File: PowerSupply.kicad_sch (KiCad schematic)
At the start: 8 parts, among them U301 TPSM33625

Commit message: Update parts
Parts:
- C301: footprint Capacitor_SMD:C_1210_3225Metric -> V2_Capacitor_SMD:C_1210; symbol Device:C_Small -> V2_Device:C_1210_10u; Manufacturer (none) -> TDK; Mouser (none) -> 810-CNA6P1X7R1H106K2; Product (none) -> CNA6P1X7R1H106K250AE; Rating (none) -> 50V; Voltage (none) -> 50V
- C302: footprint Capacitor_SMD:C_0603_1608Metric -> V2_Capacitor_SMD:C_0603; symbol Device:C_Small -> V2_Device:C_0603_0u1; Manufacturer (none) -> TDK; Mouser (none) -> 810-CGA3E2X7R1H104MA; Product (none) -> CGA3E2X7R1H104M080AA
- C303, C304: footprint Capacitor_SMD:C_1210_3225Metric -> V2_Capacitor_SMD:C_1210; symbol Device:C_Small -> V2_Device:C_1210_22u; Manufacturer (none) -> TDK; Mouser (none) -> 810-CGA6P3X7R1E226M5; Product (none) -> CGA6P3X7R1E226M250AE; Rating (none) -> 25V; Voltage (none) -> 25V
- C305: footprint Capacitor_SMD:C_0603_1608Metric -> V2_Capacitor_SMD:C_0603; symbol Device:C_Small -> V2_Device:C_0603_1u; Manufacturer (none) -> YAGEO; Mouser (none) -> 603-CC603KRX7R9BB105; Product (none) -> CC0603KRX7R9BB105
- R301: footprint Resistor_SMD:R_0603_1608Metric -> V2_Resistor_SMD:R_0603; symbol Device:R_Small -> V2_Device:R_0603_40k2; Manufacturer (none) -> Vishay; Mouser (none) -> 71-RCS060340K2FKEA; Product (none) -> RCS060340K2FKEA; Rating (none) -> 500mW
- R302: footprint Resistor_SMD:R_0603_1608Metric -> V2_Resistor_SMD:R_0603; symbol Device:R_Small -> V2_Device:R_0603_10k; Manufacturer (none) -> Vishay; Mouser (none) -> 71-CRCW060310K0FKEAC; Product (none) -> CRCW060310K0FKEAC; Rating (none) -> 100mW
- U301: Manufacturer (none) -> Texas Instruments; Mouser (none) -> 595-TPSM33625RDNR; Product (none) -> TPSM33625RDNR

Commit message: Update library
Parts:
- C301: Voltage 50V -> (none)
- C302: Rating (none) -> 50V
- C303, C304: Voltage 25V -> (none)
- C305: Manufacturer YAGEO -> TDK; Mouser 603-CC603KRX7R9BB105 -> 810-CGA3E3X7R1H105K0; Product CC0603KRX7R9BB105 -> CGA3E3X7R1H105K080AB; Rating (none) -> 50V
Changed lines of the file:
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@@
-			)
-		)
-		(property "Sim.Pin" ""
-			(at 148.59 102.87 0)
-			(effects
-				(font
-					(size 1.27 1.27)
-				)
-				(hide yes)
 			)
 		)
@@
 			)
 		)
-		(property "Sim.Pin" ""
-			(at 109.22 97.79 0)
-			(effects
-				(font
-					(size 1.27 1.27)
-				)
-				(hide yes)
-			)
-		)
 		(property "Manufacturer" "TDK"
 			(at 109.22 113.03 0)
@@
 			)
 		)
+		(property "Rating" "50V"
+			(at 109.22 120.65 0)
+			(effects
+				(font
+					(size 1.27 1.27)
+				)
+				(hide yes)
+			)
+		)
 		(pin "1"
 		)
@@
 			)
 		)
-		(property "Sim.Pin" ""
-			(at 195.58 97.79 0)
-			(effects
-				(font
-					(size 1.27 1.27)
-				)
-				(hide yes)
-			)
-		)
 		(property "Product" "CGA6P3X7R1E226M250AE"
 			(at 195.58 115.57 0)
@@
 			)
 		)
-		(property "Voltage" "25V"
-			(at 195.58 118.11 0)
-			(effects
-				(font
-					(size 1.27 1.27)
-				)
-				(hide yes)
-			)
-		)
 		(pin "1"
 		)
@@
 			)
 		)
-		(property "Sim.Pin" ""
-			(at 172.72 97.79 0)
-			(effects
-				(font
-					(size 1.27 1.27)
-				)
-				(hide yes)
-			)
-		)
 		(property "Rating" "500mW"
 			(at 172.72 118.11 0)
@@
 			)
 		)
-		(property "Description" "Power symbol creates a global label with name \"GND\" , ground"
+		(property "Description" ""
 			(at 185.42 100.33 0)
 			(effects
@@
 			)
 		)
-		(property "Description" "Power symbol creates a global label with name \"GND\" , ground"
+		(property "Description" ""
 			(at 195.58 100.33 0)
 			(effects
@@
 			)
 		)
-		(property "Description" "Power symbol creates a global label with name \"+5V\""
+		(property "Description" ""
 			(at 195.58 95.25 0)
 			(effects
@@
 			)
 		)
-		(property "Description" "Power symbol creates a global label with name \"GND\" , ground"
+		(property "Description" ""
 			(at 97.79 100.33 0)
 			(effects
@@
 			)
 		)
-		(property "Description" "Power symbol creates a global label with name \"GND\" , ground"
+		(property "Description" ""
 			(at 172.72 105.41 0)
 			(effects
@@
 			)
 		)
-		(property "Description" "Power symbol creates a global label with name \"GND\" , ground"
+		(property "Description" ""
 			(at 109.22 100.33 0)
 			(effects
@@
 			)
 		)
-		(property "Mouser" "603-CC603KRX7R9BB105"
+		(property "Mouser" "810-CGA3E3X7R1H105K0"
 			(at 128.27 125.222 0)
 			(effects
@@
 			)
 		)
-		(property "Sim.Pin" ""
-			(at 128.27 107.95 0)
-			(effects
-				(font
-					(size 1.27 1.27)
-				)
-				(hide yes)
-			)
-		)
-		(property "Product" "CC0603KRX7R9BB105"
+		(property "Product" "CGA3E3X7R1H105K080AB"
 			(at 128.27 125.73 0)
 			(effects
@@
 			)
 		)
-		(property "Manufacturer" "YAGEO"
+		(property "Manufacturer" "TDK"
 			(at 128.27 123.19 0)
+			(effects
+				(font
+					(size 1.27 1.27)
+				)
+				(hide yes)
+			)
+		)
+		(property "Rating" "50V"
+			(at 128.27 130.81 0)
 			(effects
 				(font
@@
 			)
 		)
-		(property "Sim.Pin" ""
-			(at 185.42 97.79 0)
-			(effects
-				(font
-					(size 1.27 1.27)
-				)
-				(hide yes)
-			)
-		)
 		(property "Product" "CGA6P3X7R1E226M250AE"
 			(at 185.42 115.57 0)
@@
 			)
 		)
-		(property "Voltage" "25V"
-			(at 185.42 118.11 0)
-			(effects
-				(font
-					(size 1.27 1.27)
-				)
-				(hide yes)
-			)
-		)
 		(pin "1"
 		)
@@
 			)
 		)
-		(property "Description" "Power symbol creates a global label with name \"GND\" , ground"
+		(property "Description" ""
 			(at 128.27 110.49 0)
 			(effects
@@
 			)
 		)
-		(property "Sim.Pin" ""
-			(at 172.72 102.87 0)
-			(effects
-				(font
-					(size 1.27 1.27)
-				)
-				(hide yes)
-			)
-		)
 		(property "Product" "CRCW060310K0FKEAC"
 			(at 172.72 120.65 0)
@@
 			)
 		)
-		(property "Description" "Power symbol creates a global label with name \"GND\" , ground"
+		(property "Description" ""
 			(at 148.59 115.57 0)
 			(effects
@@
 			)
 		)
-		(property "Sim.Pin" ""
-			(at 97.79 97.79 0)
-			(effects
-				(font
-					(size 1.27 1.27)
-				)
-				(hide yes)
-			)
-		)
 		(property "Product" "CNA6P1X7R1H106K250AE"
 			(at 97.79 115.57 0)
@@
 			(effects
 				(font
-					(size 1.27 1.27)
-				)
-				(hide yes)
-			)
-		)
-		(property "Voltage" "50V"
-			(at 97.79 118.11 0)
-			(effects
-				(font

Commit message: Update library
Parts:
- U301: footprint V2_Converter_DCDC:TPSM33625 -> V2_Converter_DCDC:QFN-11; symbol V2_Converter_DCDC:TPSM33625 -> V2_Converter_DCDC:TPSM33625RDNR; Rating (none) -> 2.5A
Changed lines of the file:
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@@
 	)
 	(symbol
-		(lib_id "V2_Converter_DCDC:TPSM33625")
+		(lib_id "V2_Converter_DCDC:TPSM33625RDNR")
 		(at 148.59 102.87 0)
 		(unit 1)
@@
 			)
 		)
-		(property "Footprint" "V2_Converter_DCDC:TPSM33625"
+		(property "Footprint" "V2_Converter_DCDC:QFN-11"
 			(at 148.59 118.11 0)
 			(effects
@@
 			)
 		)
-		(property "Datasheet" "https://www.ti.com/lit/ds/symlink/tpsm33625.pdf"
+		(property "Datasheet" ""
 			(at 153.67 118.11 0)
 			(effects
@@
 			(effects
 				(font
+					(size 1.27 1.27)
+				)
+				(hide yes)
+			)
+		)
+		(property "Rating" "2.5A"
+			(at 148.59 153.67 0)
+			(effects
+				(font

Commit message: Update Library
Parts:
- C301: symbol V2_Device:C_1210_10u -> V2_Capacitor:1210_10u
- C302: symbol V2_Device:C_0603_0u1 -> V2_Capacitor:0603_0u1
- C303, C304: symbol V2_Device:C_1210_22u -> V2_Capacitor:1210_22u
- C305: symbol V2_Device:C_0603_1u -> V2_Capacitor:0603_1u
- R301: symbol V2_Device:R_0603_40k2 -> V2_Resistor:0603_40k2
- R302: symbol V2_Device:R_0603_10k -> V2_Resistor:0603_10k
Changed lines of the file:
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@@
 	)
 	(symbol
-		(lib_id "V2_Device:C_0603_0u1")
+		(lib_id "V2_Capacitor:0603_0u1")
 		(at 109.22 97.79 0)
 		(unit 1)
@@
 	)
 	(symbol
-		(lib_id "V2_Device:C_1210_22u")
+		(lib_id "V2_Capacitor:1210_22u")
 		(at 195.58 97.79 0)
 		(unit 1)
@@
 	)
 	(symbol
-		(lib_id "V2_Device:R_0603_40k2")
+		(lib_id "V2_Resistor:0603_40k2")
 		(at 172.72 97.79 0)
 		(unit 1)
@@
 	)
 	(symbol
-		(lib_id "V2_Device:C_0603_1u")
+		(lib_id "V2_Capacitor:0603_1u")
 		(at 128.27 107.95 0)
 		(unit 1)
@@
 	)
 	(symbol
-		(lib_id "V2_Device:C_1210_22u")
+		(lib_id "V2_Capacitor:1210_22u")
 		(at 185.42 97.79 0)
 		(unit 1)
@@
 	)
 	(symbol
-		(lib_id "V2_Device:R_0603_10k")
+		(lib_id "V2_Resistor:0603_10k")
 		(at 172.72 102.87 0)
 		(unit 1)
@@
 	)
 	(symbol
-		(lib_id "V2_Device:C_1210_10u")
+		(lib_id "V2_Capacitor:1210_10u")
 		(at 97.79 97.79 0)
 		(unit 1)

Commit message: Replace diode
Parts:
- C301: Mouser 810-CNA6P1X7R1H106K2 -> 810-CNC6P1X7R1H106K2; Product CNA6P1X7R1H106K250AE -> CNC6P1X7R1H106K250AE
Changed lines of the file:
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@@
 			)
 		)
-		(property "Description" "Unpolarized capacitor, small symbol"
+		(property "Description" ""
 			(at 109.22 111.252 0)
 			(effects
@@
 			)
 		)
-		(property "Description" "Unpolarized capacitor, small symbol"
+		(property "Description" ""
 			(at 195.58 111.252 0)
 			(effects
@@
 			)
 		)
-		(property "Description" "Resistor, small symbol"
+		(property "Description" ""
 			(at 172.72 109.982 0)
 			(effects
@@
 		(on_board yes)
 		(dnp no)
-		(property "Reference" "#PWR0304"
+		(property "Reference" "#PWR304"
 			(at 185.42 106.68 0)
 			(effects
@@
 			(project "hihat-1"
 				(path "/6c8448b4-b04d-47e1-934e-e40cbe27a7be/db9f305d-c851-4b73-b2af-61e94839e399"
-					(reference "#PWR0304")
+					(reference "#PWR304")
 					(unit 1)
 				)
@@
 		(on_board yes)
 		(dnp no)
-		(property "Reference" "#PWR0305"
+		(property "Reference" "#PWR305"
 			(at 195.58 106.68 0)
 			(effects
@@
 			(project "hihat-1"
 				(path "/6c8448b4-b04d-47e1-934e-e40cbe27a7be/db9f305d-c851-4b73-b2af-61e94839e399"
-					(reference "#PWR0305")
+					(reference "#PWR305")
 					(unit 1)
 				)
@@
 		(on_board yes)
 		(dnp no)
-		(property "Reference" "#PWR0301"
+		(property "Reference" "#PWR301"
 			(at 195.58 99.06 0)
 			(effects
@@
 			(project "hihat-1"
 				(path "/6c8448b4-b04d-47e1-934e-e40cbe27a7be/db9f305d-c851-4b73-b2af-61e94839e399"
-					(reference "#PWR0301")
+					(reference "#PWR301")
 					(unit 1)
 				)
@@
 		(on_board yes)
 		(dnp no)
-		(property "Reference" "#PWR0302"
+		(property "Reference" "#PWR302"
 			(at 97.79 106.68 0)
 			(effects
@@
 			(project "hihat-1"
 				(path "/6c8448b4-b04d-47e1-934e-e40cbe27a7be/db9f305d-c851-4b73-b2af-61e94839e399"
-					(reference "#PWR0302")
+					(reference "#PWR302")
 					(unit 1)
 				)
@@
 		(on_board yes)
 		(dnp no)
-		(property "Reference" "#PWR0306"
+		(property "Reference" "#PWR306"
 			(at 172.72 111.76 0)
 			(effects
@@
 			(project "hihat-1"
 				(path "/6c8448b4-b04d-47e1-934e-e40cbe27a7be/db9f305d-c851-4b73-b2af-61e94839e399"
-					(reference "#PWR0306")
+					(reference "#PWR306")
 					(unit 1)
 				)
@@
 		(on_board yes)
 		(dnp no)
-		(property "Reference" "#PWR0303"
+		(property "Reference" "#PWR303"
 			(at 109.22 106.68 0)
 			(effects
@@
 			(project "hihat-1"
 				(path "/6c8448b4-b04d-47e1-934e-e40cbe27a7be/db9f305d-c851-4b73-b2af-61e94839e399"
-					(reference "#PWR0303")
+					(reference "#PWR303")
 					(unit 1)
 				)
@@
 			)
 		)
-		(property "Description" "Unpolarized capacitor, small symbol"
+		(property "Description" ""
 			(at 128.27 121.412 0)
 			(effects
@@
 			)
 		)
-		(property "Description" "Unpolarized capacitor, small symbol"
+		(property "Description" ""
 			(at 185.42 111.252 0)
 			(effects
@@
 		(on_board yes)
 		(dnp no)
-		(property "Reference" "#PWR0307"
+		(property "Reference" "#PWR307"
 			(at 128.27 116.84 0)
 			(effects
@@
 			(project "hihat-1"
 				(path "/6c8448b4-b04d-47e1-934e-e40cbe27a7be/db9f305d-c851-4b73-b2af-61e94839e399"
-					(reference "#PWR0307")
+					(reference "#PWR307")
 					(unit 1)
 				)
@@
 			)
 		)
-		(property "Description" "Resistor, small symbol"
+		(property "Description" ""
 			(at 172.72 115.062 0)
 			(effects
@@
 		(on_board yes)
 		(dnp no)
-		(property "Reference" "#PWR0308"
+		(property "Reference" "#PWR308"
 			(at 148.59 121.92 0)
 			(effects
@@
 			(project "hihat-1"
 				(path "/6c8448b4-b04d-47e1-934e-e40cbe27a7be/db9f305d-c851-4b73-b2af-61e94839e399"
-					(reference "#PWR0308")
+					(reference "#PWR308")
 					(unit 1)
 				)
@@
 			)
 		)
-		(property "Description" "Unpolarized capacitor, small symbol"
+		(property "Description" ""
 			(at 97.79 111.252 0)
 			(effects
@@
 			)
 		)
-		(property "Mouser" "810-CNA6P1X7R1H106K2"
+		(property "Mouser" "810-CNC6P1X7R1H106K2"
 			(at 97.79 114.3 0)
 			(effects
@@
 			)
 		)
-		(property "Product" "CNA6P1X7R1H106K250AE"
+		(property "Product" "CNC6P1X7R1H106K250AE"
 			(at 97.79 115.57 0)
 			(effects

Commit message: Replace diode
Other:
- title: Power Supply -> V2 drum

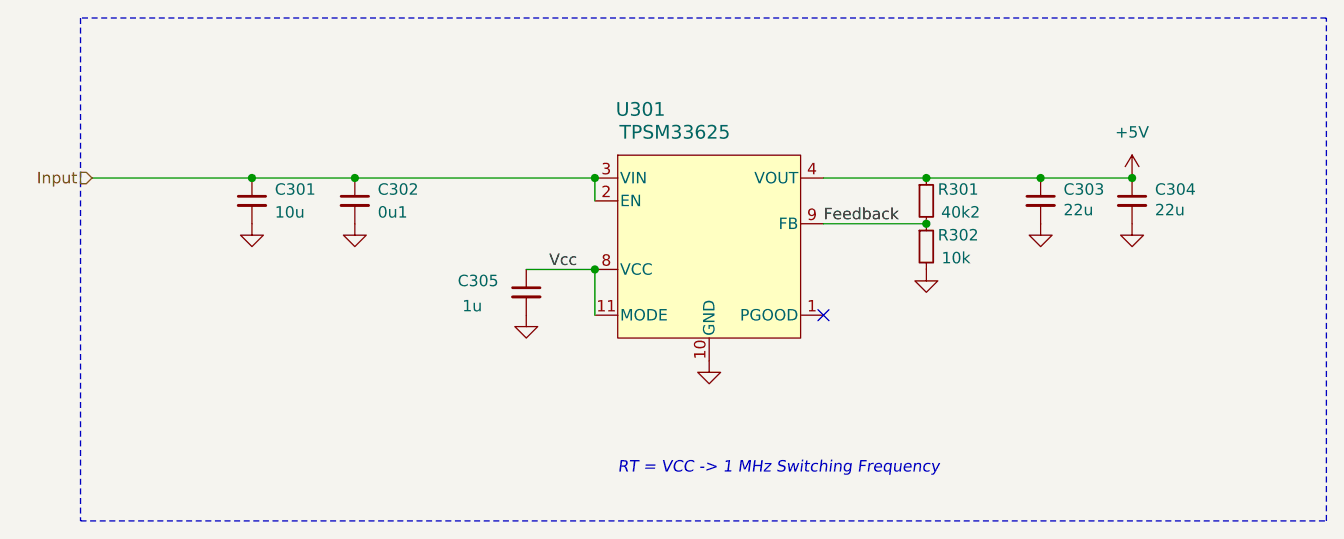
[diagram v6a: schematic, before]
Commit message: Replace step-down
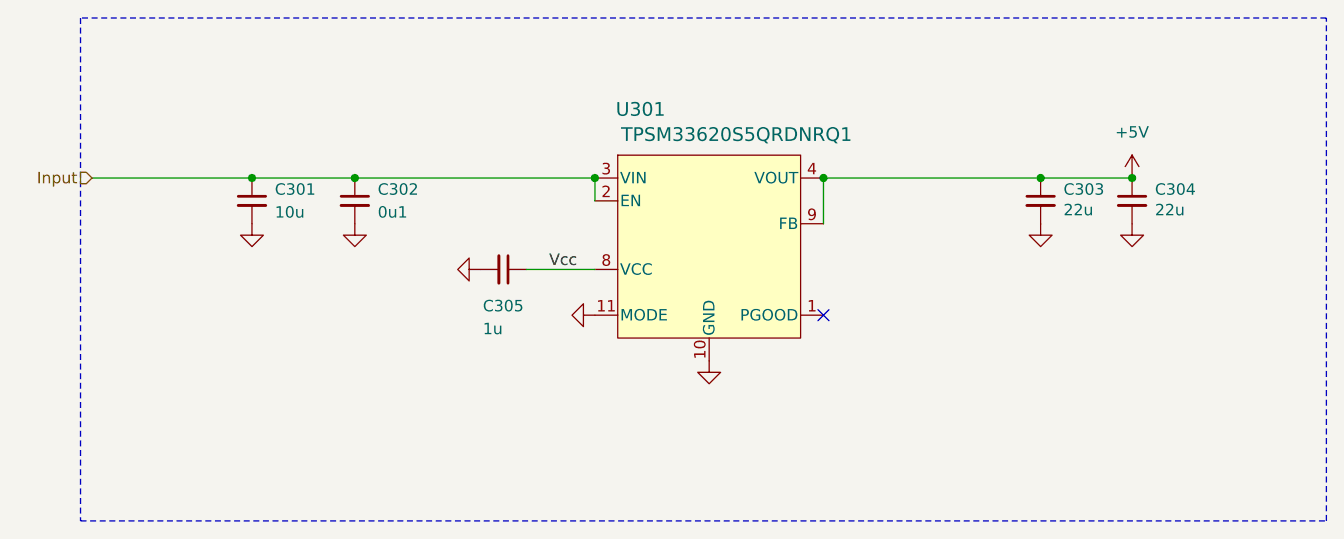
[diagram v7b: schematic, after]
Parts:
- removed R301: 40k2, V2_Resistor_SMD:R_0603, symbol V2_Resistor:0603_40k2
- removed R302: 10k, V2_Resistor_SMD:R_0603, symbol V2_Resistor:0603_10k
- U301: value TPSM33625 -> TPSM33620S5QRDNRQ1; symbol V2_Converter_DCDC:TPSM33625RDNR -> V2_Converter_DCDC:TPSM33620S5QRDNRQ1; Mouser 595-TPSM33625RDNR -> 595-SM33620S5QRDNRQ1; Product TPSM33625RDNR -> TPSM33620S5QRDNRQ1; Rating 2.5A -> 2A
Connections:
- net Feedback is gone; now on net +5V: U301.9 (FB)
- net GND: now also U301.11 (MODE)
- net Vcc: no longer U301.11 (MODE)
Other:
- note removed: "RT = VCC -> 1 MHz Switching Frequency"
- moved on the sheet: C305

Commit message: Update
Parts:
- C301, C302: Id (none) -> Capacitor:${SYMBOL_NAME}
- C303: renamed from C305; Id (none) -> Capacitor:${SYMBOL_NAME}
- C304: renamed from C303; Id (none) -> Capacitor:${SYMBOL_NAME}
- C305: renamed from C304; Id (none) -> Capacitor:${SYMBOL_NAME}
- U301: Id (none) -> DCDC:${SYMBOL_NAME}
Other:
- company: +5V -> Versio Duo
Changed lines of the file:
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@@
 	(title_block
 		(title "V2 drum")
-		(date "2026-03-30")
+		(date "2026-04-14")
 		(rev "2026-03-30")
-		(company "+5V")
+		(company "Versio Duo")
+		(comment 1 "Percussion Controller")
 	)
 	(junction
@@
 			)
 		)
+		(property "Id" "DCDC:${SYMBOL_NAME}"
+			(at 148.59 147.32 0)
+			(hide yes)
+			(show_name no)
+			(do_not_autoplace no)
+			(effects
+				(font
+					(size 1.27 1.27)
+				)
+			)
+		)
 		(pin "1"
 		)
@@
 			)
 		)
+		(property "Id" "Capacitor:${SYMBOL_NAME}"
+			(at 109.22 113.03 0)
+			(hide yes)
+			(show_name no)
+			(do_not_autoplace no)
+			(effects
+				(font
+					(size 1.27 1.27)
+				)
+			)
+		)
 		(pin "1"
 		)
@@
 		(in_pos_files yes)
 		(dnp no)
-		(property "Reference" "C304"
+		(property "Reference" "C305"
 			(at 198.12 96.52 0)
 			(show_name no)
@@
 		)
 		(property "Manufacturer" "TDK"
+			(at 195.58 113.03 0)
+			(hide yes)
+			(show_name no)
+			(do_not_autoplace no)
+			(effects
+				(font
+					(size 1.27 1.27)
+				)
+			)
+		)
+		(property "Id" "Capacitor:${SYMBOL_NAME}"
 			(at 195.58 113.03 0)
 			(hide yes)
@@
 			(project "drum"
 				(path "/6c8448b4-b04d-47e1-934e-e40cbe27a7be/db9f305d-c851-4b73-b2af-61e94839e399"
-					(reference "C304")
+					(reference "C305")
 					(unit 1)
 				)
@@
 		(in_pos_files yes)
 		(dnp no)
-		(property "Reference" "#PWR304"
+		(property "Reference" "#PWR0306"
 			(at 185.42 106.68 0)
 			(hide yes)
@@
 			(project "drum"
 				(path "/6c8448b4-b04d-47e1-934e-e40cbe27a7be/db9f305d-c851-4b73-b2af-61e94839e399"
-					(reference "#PWR304")
+					(reference "#PWR0306")
 					(unit 1)
 				)
@@
 		(in_pos_files yes)
 		(dnp no)
-		(property "Reference" "#PWR305"
+		(property "Reference" "#PWR0308"
 			(at 195.58 106.68 0)
 			(hide yes)
@@
 			(project "drum"
 				(path "/6c8448b4-b04d-47e1-934e-e40cbe27a7be/db9f305d-c851-4b73-b2af-61e94839e399"
-					(reference "#PWR305")
+					(reference "#PWR0308")
 					(unit 1)
 				)
@@
 		(in_pos_files yes)
 		(dnp no)
-		(property "Reference" "#PWR301"
+		(property "Reference" "#PWR0307"
 			(at 195.58 99.06 0)
 			(hide yes)
@@
 			(project "drum"
 				(path "/6c8448b4-b04d-47e1-934e-e40cbe27a7be/db9f305d-c851-4b73-b2af-61e94839e399"
-					(reference "#PWR301")
+					(reference "#PWR0307")
 					(unit 1)
 				)
@@
 		(in_pos_files yes)
 		(dnp no)
-		(property "Reference" "#PWR302"
+		(property "Reference" "#PWR0301"
 			(at 97.79 106.68 0)
 			(hide yes)
@@
 			(project "drum"
 				(path "/6c8448b4-b04d-47e1-934e-e40cbe27a7be/db9f305d-c851-4b73-b2af-61e94839e399"
-					(reference "#PWR302")
+					(reference "#PWR0301")
 					(unit 1)
 				)
@@
 		(in_pos_files yes)
 		(dnp no)
-		(property "Reference" "#PWR303"
+		(property "Reference" "#PWR0302"
 			(at 109.22 106.68 0)
 			(hide yes)
@@
 			(project "drum"
 				(path "/6c8448b4-b04d-47e1-934e-e40cbe27a7be/db9f305d-c851-4b73-b2af-61e94839e399"
-					(reference "#PWR303")
+					(reference "#PWR0302")
 					(unit 1)
 				)
@@
 		(in_pos_files yes)
 		(dnp no)
-		(property "Reference" "C305"
+		(property "Reference" "C303"
 			(at 123.444 109.474 90)
 			(show_name no)
@@
 		(property "Rating" "50V"
 			(at 102.87 105.41 0)
+			(hide yes)
+			(show_name no)
+			(do_not_autoplace no)
+			(effects
+				(font
+					(size 1.27 1.27)
+				)
+			)
+		)
+		(property "Id" "Capacitor:${SYMBOL_NAME}"
+			(at 110.49 105.41 0)
 			(hide yes)
 			(show_name no)
@@
 			(project "drum"
 				(path "/6c8448b4-b04d-47e1-934e-e40cbe27a7be/db9f305d-c851-4b73-b2af-61e94839e399"
-					(reference "C305")
+					(reference "C303")
 					(unit 1)
 				)
@@
 		(in_pos_files yes)
 		(dnp no)
-		(property "Reference" "C303"
+		(property "Reference" "C304"
 			(at 187.96 96.52 0)
 			(show_name no)
@@
 		)
 		(property "Manufacturer" "TDK"
+			(at 185.42 113.03 0)
+			(hide yes)
+			(show_name no)
+			(do_not_autoplace no)
+			(effects
+				(font
+					(size 1.27 1.27)
+				)
+			)
+		)
+		(property "Id" "Capacitor:${SYMBOL_NAME}"
 			(at 185.42 113.03 0)
 			(hide yes)
@@
 			(project "drum"
 				(path "/6c8448b4-b04d-47e1-934e-e40cbe27a7be/db9f305d-c851-4b73-b2af-61e94839e399"
-					(reference "C303")
+					(reference "C304")
 					(unit 1)
 				)
@@
 		(in_pos_files yes)
 		(dnp no)
-		(property "Reference" "#PWR307"
+		(property "Reference" "#PWR0303"
 			(at 116.84 105.41 0)
 			(hide yes)
@@
 			(project "drum"
 				(path "/6c8448b4-b04d-47e1-934e-e40cbe27a7be/db9f305d-c851-4b73-b2af-61e94839e399"
-					(reference "#PWR307")
+					(reference "#PWR0303")
 					(unit 1)
 				)
@@
 		(in_pos_files yes)
 		(dnp no)
-		(property "Reference" "#PWR308"
+		(property "Reference" "#PWR0305"
 			(at 148.59 121.92 0)
 			(hide yes)
@@
 			(project "drum"
 				(path "/6c8448b4-b04d-47e1-934e-e40cbe27a7be/db9f305d-c851-4b73-b2af-61e94839e399"
-					(reference "#PWR308")
+					(reference "#PWR0305")
 					(unit 1)
 				)
@@
 			)
 		)
+		(property "Id" "Capacitor:${SYMBOL_NAME}"
+			(at 97.79 113.03 0)
+			(hide yes)
+			(show_name no)
+			(do_not_autoplace no)
+			(effects
+				(font
+					(size 1.27 1.27)
+				)
+			)
+		)
 		(pin "1"
 		)
@@
 		(in_pos_files yes)
 		(dnp no)
-		(property "Reference" "#PWR0309"
+		(property "Reference" "#PWR0304"
 			(at 129.54 110.49 0)
 			(hide yes)
@@
 			(project "drum"
 				(path "/6c8448b4-b04d-47e1-934e-e40cbe27a7be/db9f305d-c851-4b73-b2af-61e94839e399"
-					(reference "#PWR0309")
+					(reference "#PWR0304")
 					(unit 1)
 				)
